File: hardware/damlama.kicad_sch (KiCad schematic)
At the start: 0 parts

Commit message: Beta Finished
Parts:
- added H1, H2, H3, H4: MountingHole, MountingHole:MountingHole_2.5mm, symbol Mechanical:MountingHole
- added J4: PJ-002A, Damlama:CUI_PJ-002A, symbol Damlama:PJ-002A
- added J5: RELAY, Connector_Phoenix_MC:PhoenixContact_MC_1,5_3-G-3.5_1x03_P3.50mm_Horizontal, symbol Connector_Generic:Conn_01x03
- added J6: SENSOR, Connector_Phoenix_MC:PhoenixContact_MC_1,5_3-G-3.5_1x03_P3.50mm_Horizontal, symbol Connector_Generic:Conn_01x03
- added J8: 629105150521, Damlama:CONN_USB_WURTH_629105150521, symbol Damlama:629105150521
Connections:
- new net +5V: J6.1 (Pin_1)
- new net ADC/SENSOR: J6.2 (Pin_2)
- new net GND: J4.2, J4.3, J6.3 (Pin_3), J8.5
- new net MCU/USB_DM: J8.2
- new net MCU/USB_DP: J8.3
- new net Power/VIN: J4.1
- new net RELAY/RLIN: J5.2 (Pin_2)
- new net RELAY/RLNC: J5.3 (Pin_3)
- new net RELAY/RLNO: J5.1 (Pin_1)
- no-connect marks 0 -> 2
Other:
- added sheet ADC (adc.kicad_sch)
- added sheet GSM (gsm.kicad_sch)
- added sheet MCU (mcu.kicad_sch)
- added sheet Power (power.kicad_sch)
- added sheet RELAY (relay.kicad_sch)
- note added: "MOUNTING HOLES"

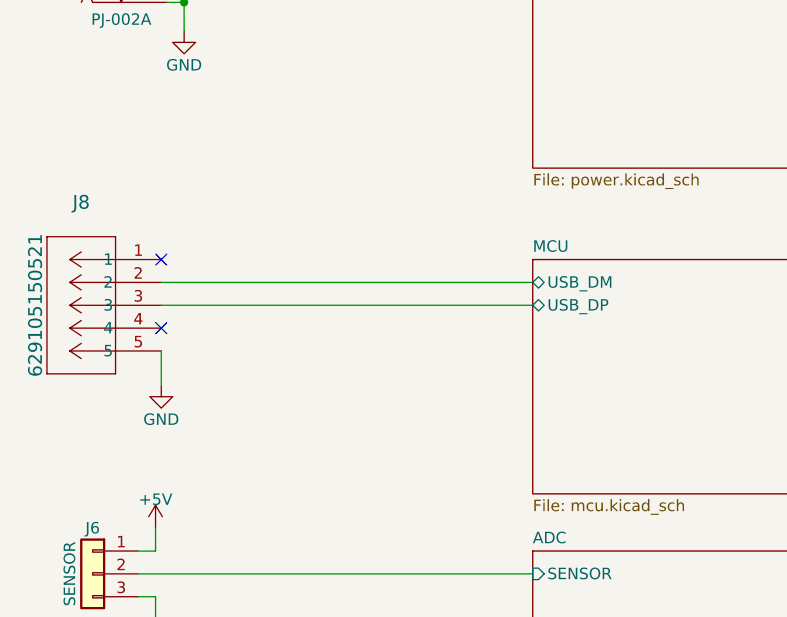
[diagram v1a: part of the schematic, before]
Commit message: MCU BOOT0 mistake fixed
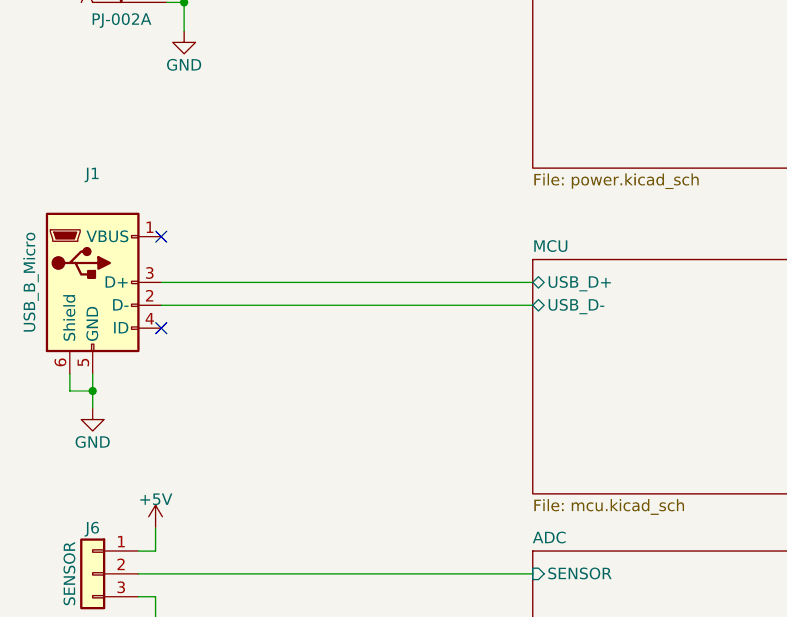
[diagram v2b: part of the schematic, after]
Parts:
- removed J8: 629105150521, Damlama:CONN_USB_WURTH_629105150521, symbol Damlama:629105150521
- added J1: USB_B_Micro, Connector_USB:USB_Micro-B_Molex_47346-0001, symbol Connector:USB_B_Micro
- H1, H2, H3, H4: now left out of the parts list
- J5, J6: footprint Connector_Phoenix_MC:PhoenixContact_MC_1,5_3-G-3.5_1x03_P3.50mm_Horizontal -> Connector_Phoenix_MSTB:PhoenixContact_MSTBA_2,5_3-G-5,08_1x03_P5.08mm_Horizontal; now left out of the parts list
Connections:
- net GND: now also J1.5 (GND), J1.6 (Shield)
- new net MCU/USB_D+: J1.3 (D+)
- new net MCU/USB_D-: J1.2 (D-)
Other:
- sheet MCU ports: added USB_D+, USB_D-; removed USB_DM, USB_DP
